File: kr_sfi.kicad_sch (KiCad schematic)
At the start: 85 parts, among them U37 NTS0102_TSSOP, U39 TLK10232CTR, Y2 Oscillator_156.25MHz_SG3225EEN

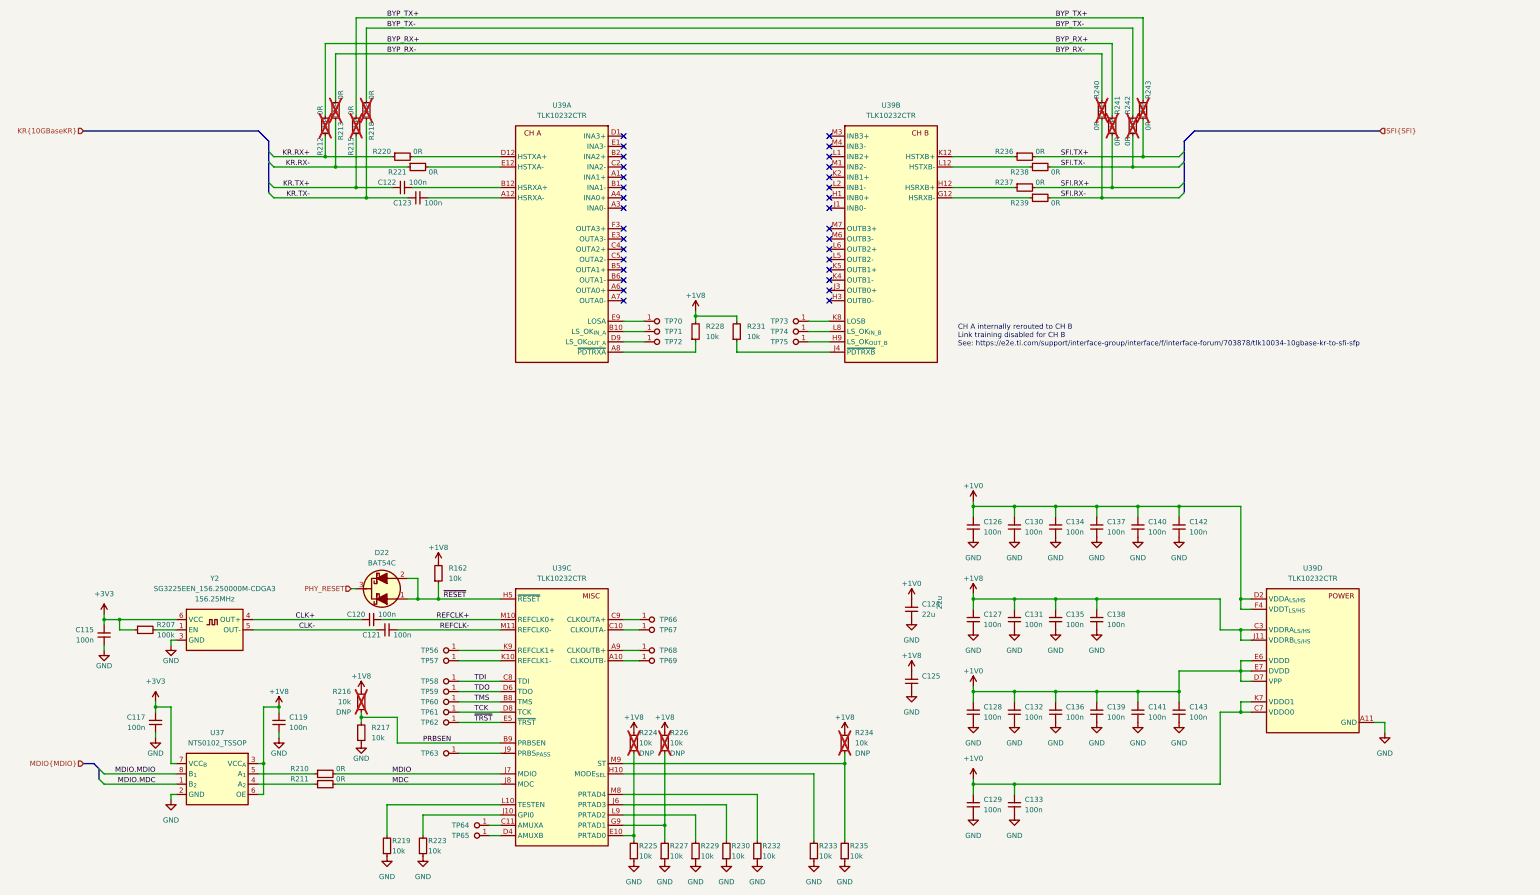
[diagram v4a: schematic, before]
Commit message: Reannotate schematic
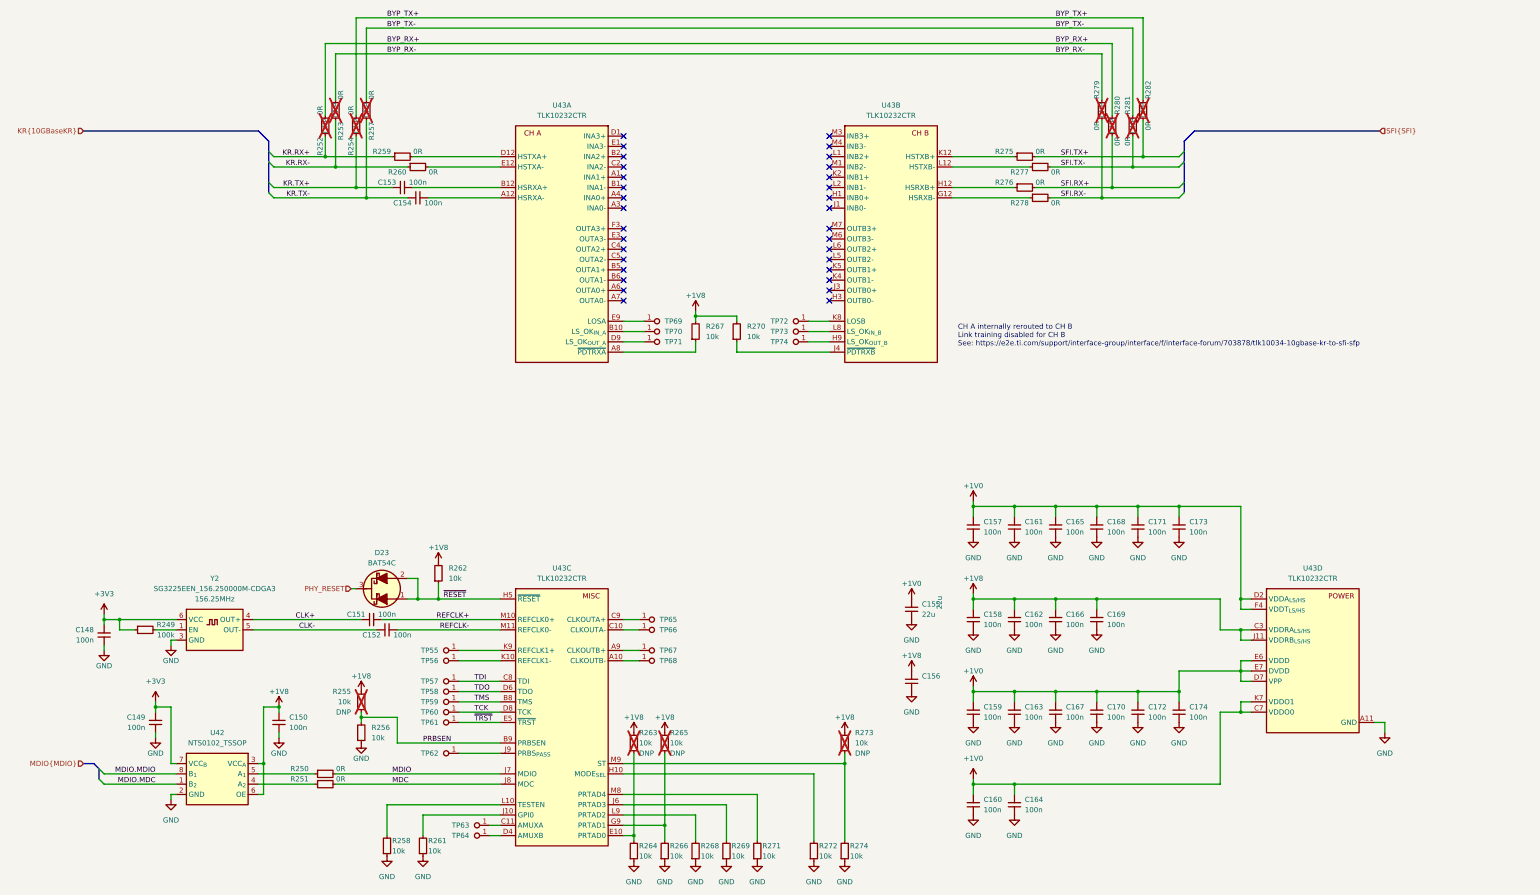
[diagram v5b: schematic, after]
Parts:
- renumbered C115 to C148, C117 to C149, C119 to C150, C120 to C151, C121 to C152, C122 to C153, C123 to C154, C124 to C155, C125 to C156, C126 to C157, C127 to C158, C128 to C159, C129 to C160, C130 to C161, C131 to C162, C132 to C163, C133 to C164, C134 to C165, C135 to C166, C136 to C167, C137 to C168, C138 to C169, C139 to C170, C140 to C171, C141 to C172, C142 to C173, C143 to C174, D22 to D23, R207 to R249, R210 to R250, R211 to R251, R212 to R252, R213 to R253, R215 to R254, R216 to R255, R217 to R256, R218 to R257, R219 to R258, R220 to R259, R221 to R260, R223 to R261, R162 to R262, R224 to R263, R225 to R264, R226 to R265, R227 to R266, R228 to R267, R229 to R268, R230 to R269, R231 to R270, R232 to R271, R233 to R272, R234 to R273, R235 to R274, R236 to R275, R237 to R276, R238 to R277, R239 to R278, R240 to R279, R241 to R280, R242 to R281, R243 to R282, TP56 to TP55, TP57 to TP56, TP58 to TP57, TP59 to TP58, TP60 to TP59, TP61 to TP60, TP62 to TP61, TP63 to TP62, TP64 to TP63, TP65 to TP64, TP66 to TP65, TP67 to TP66, TP68 to TP67, TP69 to TP68, TP70 to TP69, TP71 to TP70, TP72 to TP71, TP73 to TP72, TP74 to TP73, TP75 to TP74, U37 to U42, U39 to U43

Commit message: Optimize BOM, reannotate
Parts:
- renumbered R249 to R246, R250 to R247, R251 to R248, R252 to R249, R253 to R250, R254 to R251, R255 to R252, R256 to R253, R257 to R254, R258 to R255, R259 to R256, R260 to R257, R261 to R258, R262 to R259, R263 to R260, R264 to R261, R265 to R262, R266 to R263, R267 to R264, R268 to R265, R269 to R266, R270 to R267, R271 to R268, R272 to R269, R273 to R270, R274 to R271, R275 to R272, R276 to R273, R277 to R274, R278 to R275, R279 to R276, R280 to R277, R281 to R278, R282 to R279, TP55 to TP57, TP56 to TP58, TP57 to TP59, TP58 to TP60, TP59 to TP61, TP60 to TP62, TP61 to TP63, TP62 to TP64, TP63 to TP65, TP64 to TP66, TP65 to TP67, TP66 to TP68, TP67 to TP69, TP68 to TP70, TP69 to TP71, TP70 to TP72, TP71 to TP73, TP72 to TP74, TP73 to TP75, TP74 to TP76

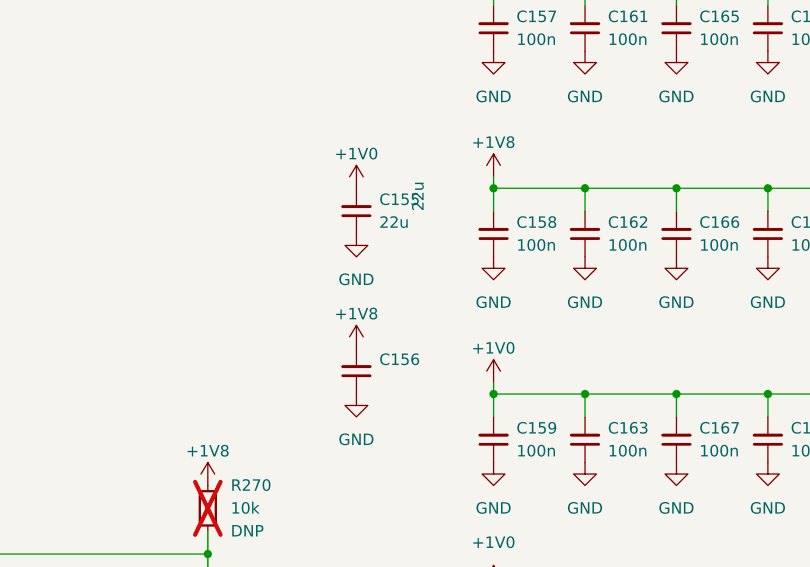
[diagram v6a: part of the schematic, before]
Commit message: [#58904] Fix DRC
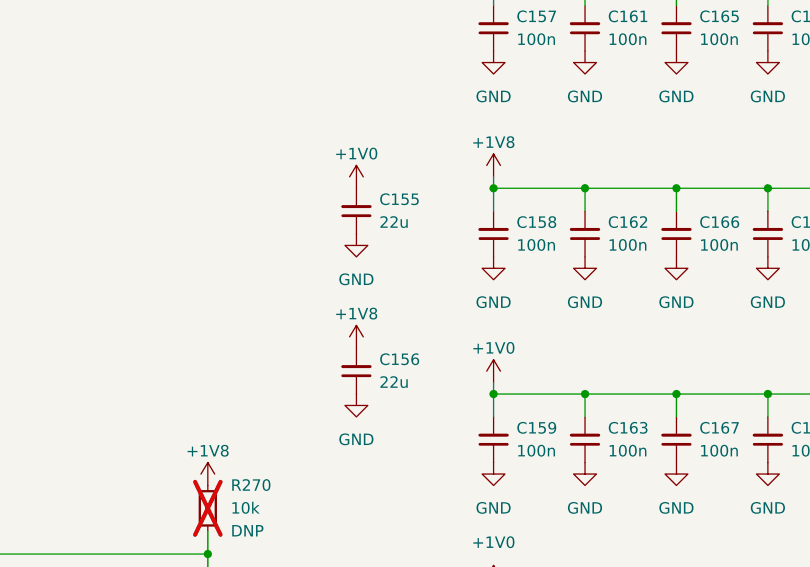
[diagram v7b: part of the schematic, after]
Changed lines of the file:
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@@
   )
   (symbol (lib_id "antmicroCapacitors0603:C_22u_16V_0603") (at 261.62 208.28 90) (unit 1)
-    (in_bom yes) (on_board yes) (dnp no)
-    (property "Reference" "C156" (at 264.16 204.4636 90)
+    (in_bom yes) (on_board yes) (dnp no) (fields_autoplaced)
+    (property "Reference" "C156" (at 264.16 204.4635 90)
       (effects (font (size 1.27 1.27) (thickness 0.15)) (justify right))
     )
@@
       (effects (font (size 1.27 1.27) (thickness 0.15)) (justify left bottom) hide)
     )
-    (property "Val" "22u" (at 269.24 187.96 0)
-      (effects (font (size 1.27 1.27) (thickness 0.15)) (justify left bottom))
+    (property "Val" "22u" (at 264.16 207.0035 90)
+      (effects (font (size 1.27 1.27) (thickness 0.15)) (justify right))
     )
     (property "Voltage" "16V" (at 289.56 187.96 0)

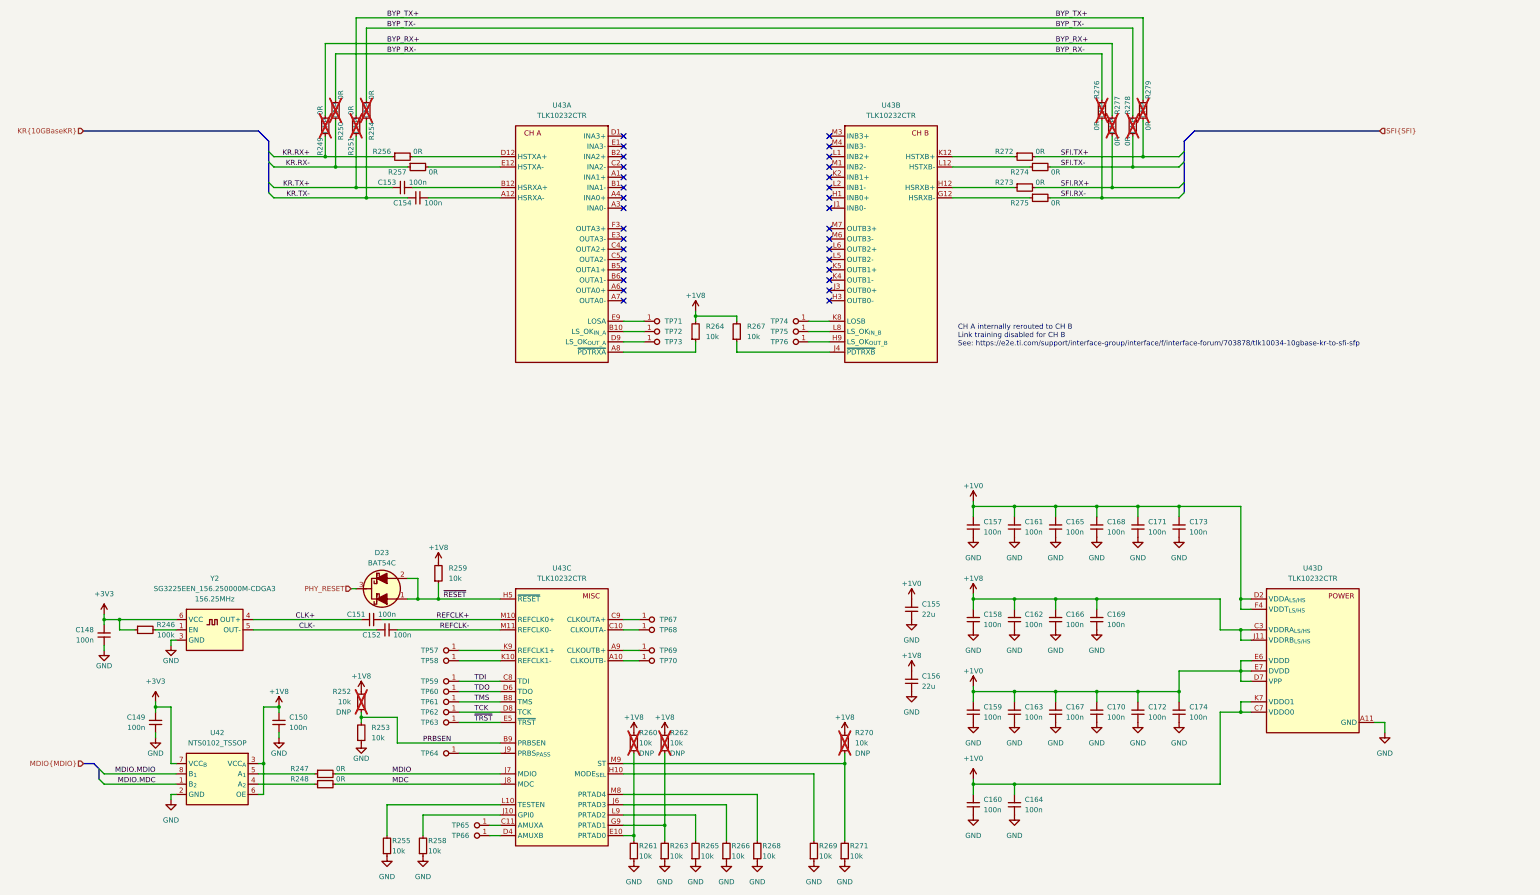
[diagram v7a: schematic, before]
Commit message: Update components from the library
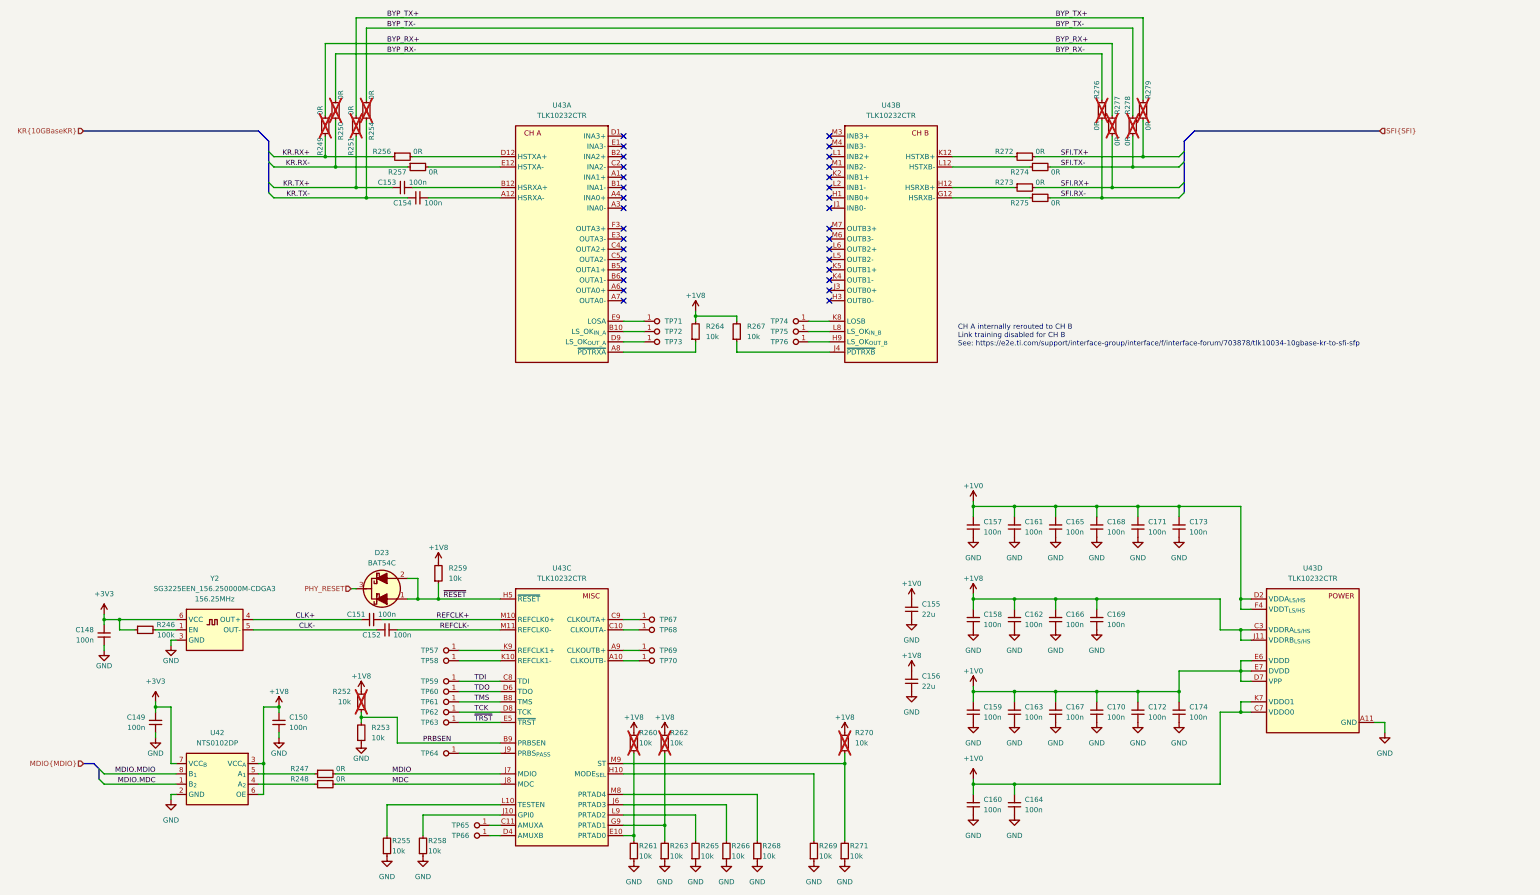
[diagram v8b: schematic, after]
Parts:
- C148, C149, C150, C151, C152, C153, C154, C155, C156, C157, C158, C159, C160, C161, C162, C163, C164, C165, C166, C167, C168, C169, C170, C171, C172, C173, C174, R246, R247, R248, R253, R255, R256, R257, R258, R259, R261, R263, R264, R265, R266, R267, R268, R269, R271, R272, R273, R274, R275, TP57, TP58, TP59, TP60, TP61, TP62, TP63, TP64, TP65, TP66, TP67, TP68, TP69, TP70, TP71, TP72, TP73, TP74, TP75, TP76, Y2: Public (none) -> False
- R249, R250, R251, R252, R254, R260, R262, R270, R276, R277, R278, R279: DNP DNP -> (none); Public (none) -> False
